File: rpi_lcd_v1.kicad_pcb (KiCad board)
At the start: 2 copper layers, 43.5 x 53 mm, 19 parts, among them J1 RPI GPIO, P1 CONN_9

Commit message: Routed
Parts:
- gave numbers to parts that had none: 2
- renumbered VAL to osh1, VAL to rohm1
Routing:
- net GND: track 0.00 -> 159.4 mm
- net N-0000028: track 0.00 -> 86.5 mm, vias 0 -> 1
- net N-0000032: track 0.00 -> 50.8 mm
- net SW_4: track 0.00 -> 49.0 mm
- net N-0000031: track 0.00 -> 44.3 mm, vias 0 -> 2
- net SW_3: track 0.00 -> 43.2 mm
- net SW_1: track 0.00 -> 41.1 mm
- net SW_2: track 0.00 -> 39.1 mm
- net +3.3V: track 0.00 -> 29.9 mm, vias 0 -> 1
- net N-000008: track 0.00 -> 25.7 mm
- net RST: track 0.00 -> 22.4 mm, vias 0 -> 1
- net SCE: track 0.00 -> 15.5 mm
- net SCLK: track 0.00 -> 10.8 mm
- net SDIN: track 0.00 -> 6.72 mm
- net N-0000030: track 0.00 -> 4.19 mm
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
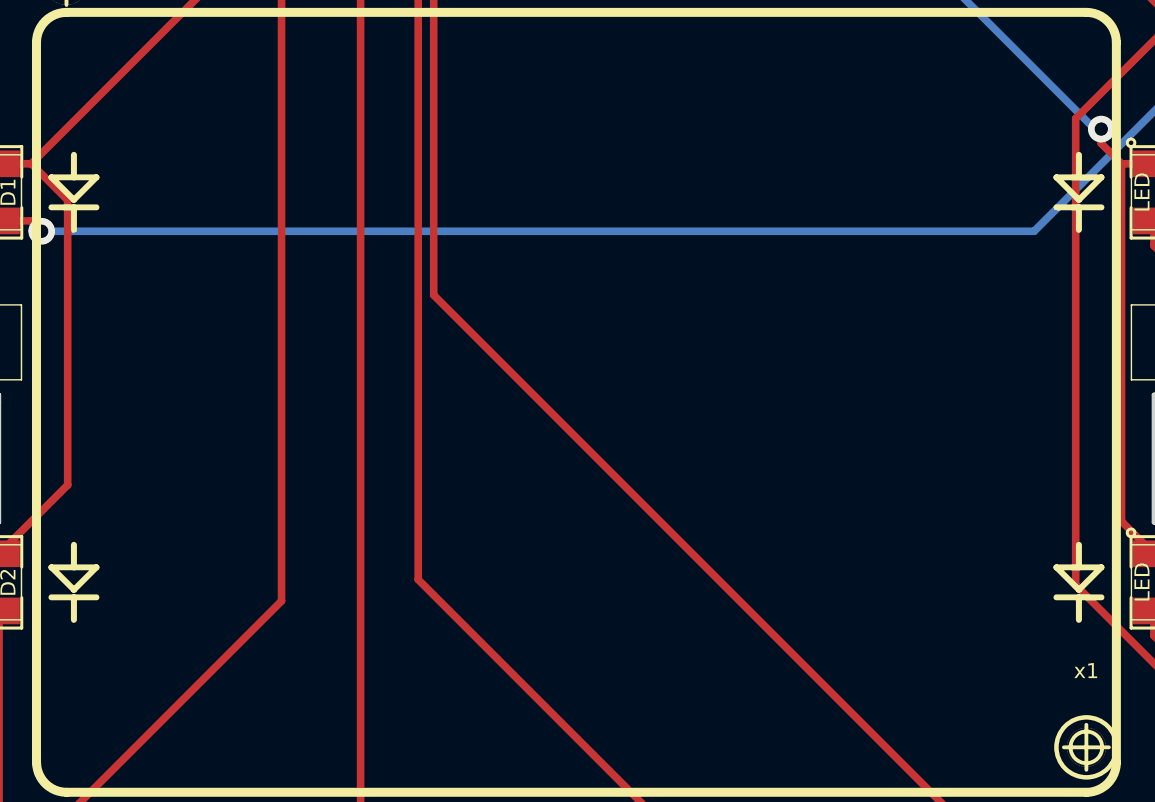
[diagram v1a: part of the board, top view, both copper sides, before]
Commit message: Add silk screen
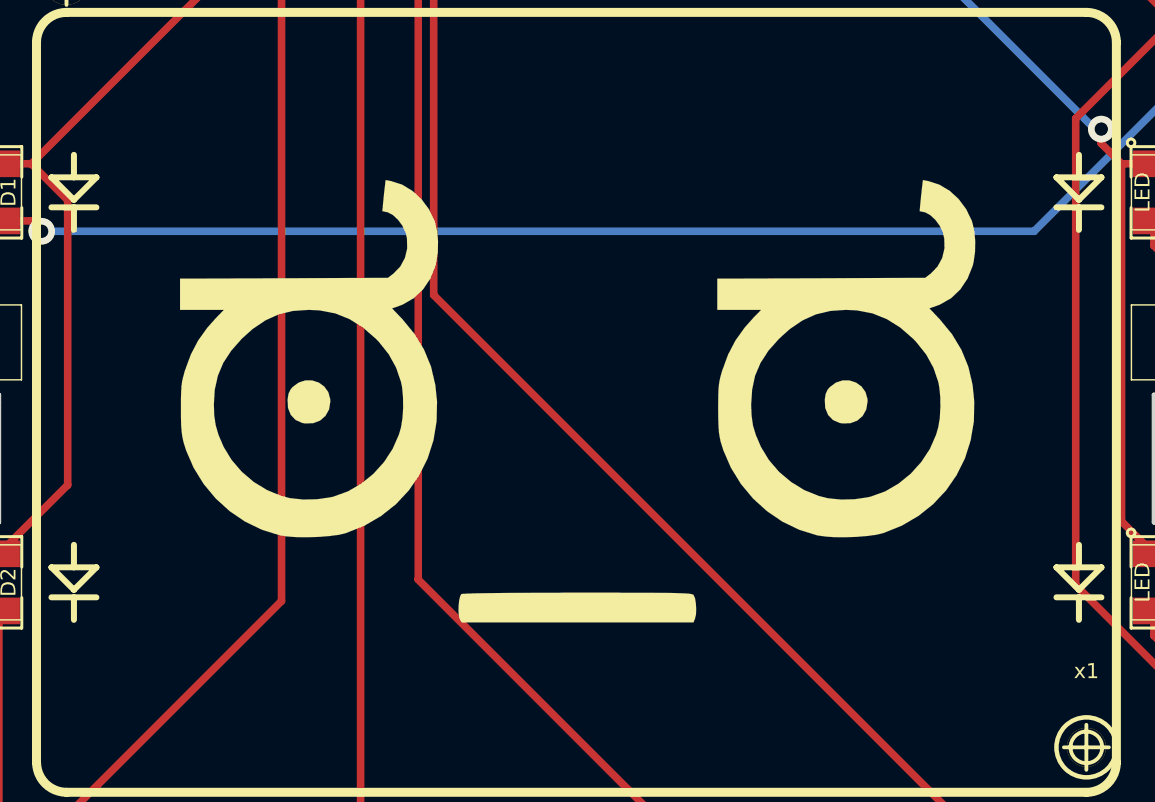
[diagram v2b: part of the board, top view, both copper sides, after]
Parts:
- added VAL: look_of_disapproval_scaled, look_of_disapproval_scaled, F.Cu at (259.1, 142.2)
- added VAL: back_scaled, back_scaled, F.Cu at (259.7, 141.0)

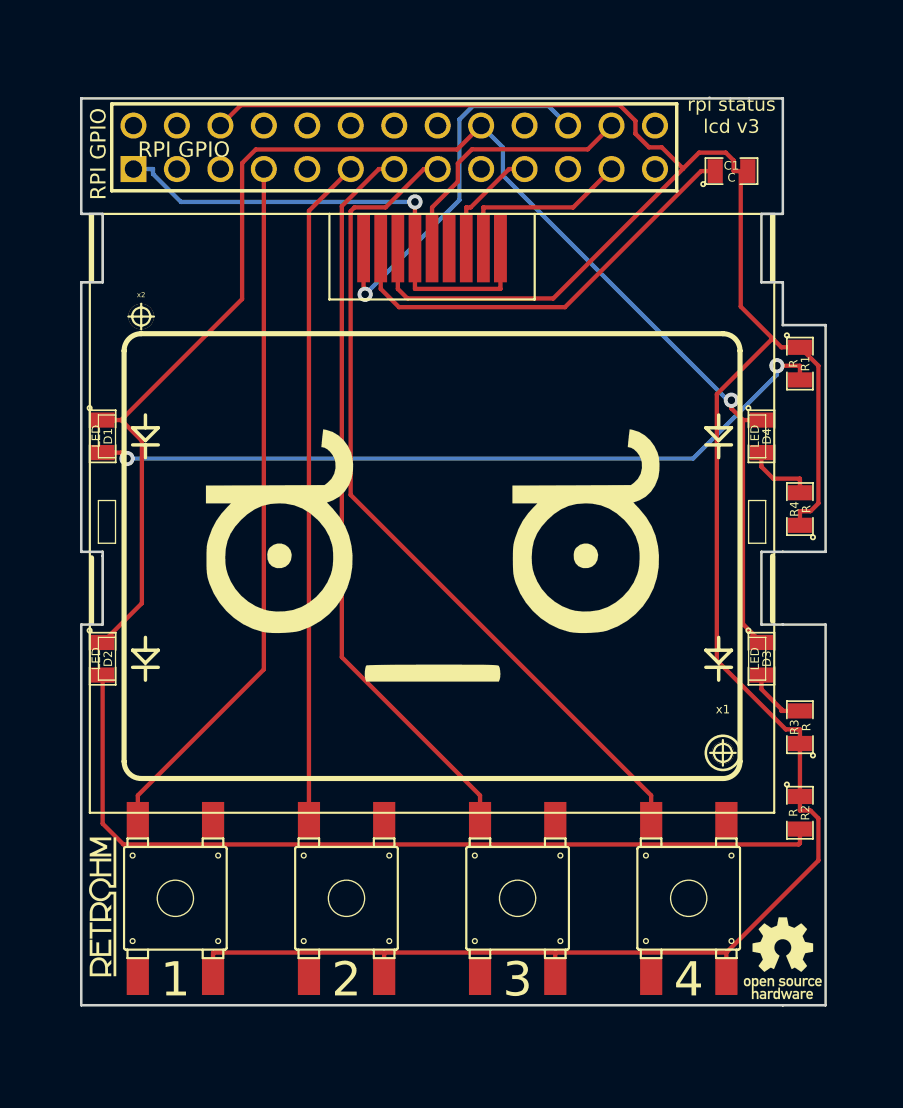
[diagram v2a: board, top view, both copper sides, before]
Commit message: Added ground plane fill
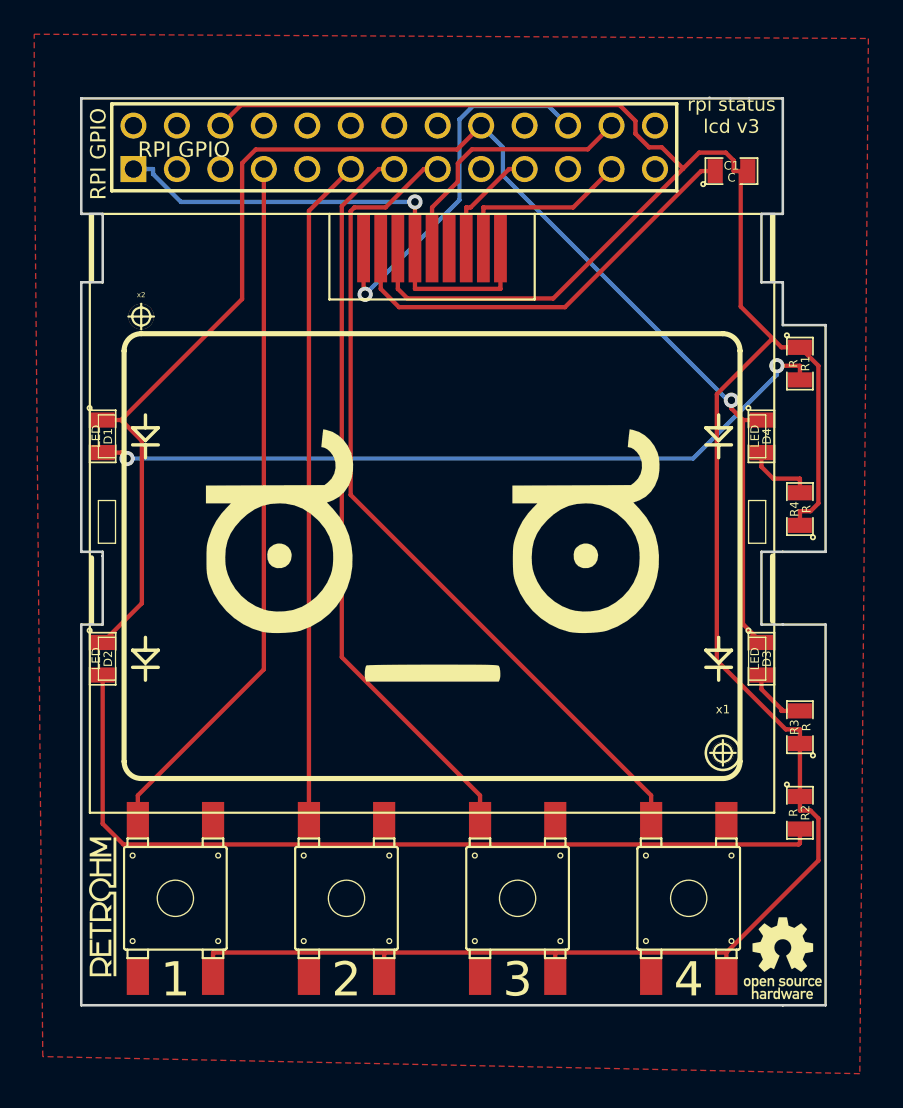
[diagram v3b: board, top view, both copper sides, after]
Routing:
- added copper zone on F.Cu, net GND
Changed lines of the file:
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@@
-(kicad_pcb (version 3) (host pcbnew "(2013-feb-26)-stable")
+(kicad_pcb (version 3) (host pcbnew "(2013-mar-13)-testing")
   (general
     (links 29)
@@
   (segment (start 259.08 119.38) (end 258.2741 119.38) (width 0.254) (layer F.Cu) (net 16))
   (segment (start 271.5554 157.4178) (end 271.5554 155.9875) (width 0.254) (layer F.Cu) (net 16))
+  (zone (net 2) (net_name GND) (layer F.Cu) (hatch edge 0.508)
+    (connect_pads (clearance 0.508))
+    (min_thickness 0.254)
+    (fill (arc_segments 16) (thermal_gap 0.508) (thermal_bridge_width 0.508))
+    (polygon
+      (pts
+        (xy 235.5 111.5) (xy 284.25 111.75) (xy 283.75 172.25) (xy 236 171.25) (xy 235.5 116.25)
+      )
+    )
+  )
 )
